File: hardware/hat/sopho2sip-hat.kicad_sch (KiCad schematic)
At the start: 52 parts, among them J1 Raspberry Pi GPIO, J2 D340 Audio, J3 D340 PC-Schnittstelle, SW1 Taste, T1 600:600, T2 600:600, U1 24LC32, U2 WM8731SEDS, U3 ADuM5211, U4 AP2112K-3.3, U5 MAX3232E, Y1 12.288MHz

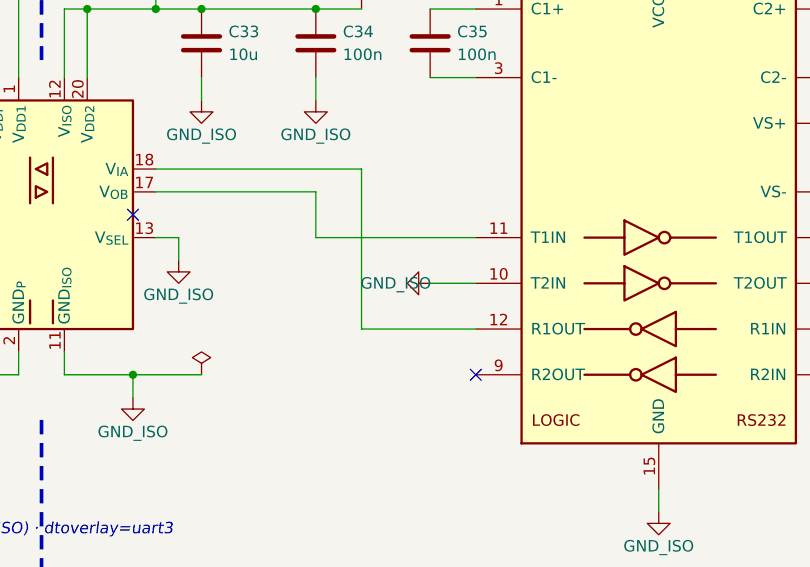
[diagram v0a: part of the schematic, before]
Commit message: CM4-Träger: hierarchischer KiCad-Schaltplan; gemeinsamer Generator kicadgen
- hardware/kicadgen.py: Symbole, Leitungen, hierarchische Blätter mit Blattpins,
  Projektbibliothek für eigene Symbole, Prüfung (ERC + Pin-Gruppen gegen SOLL)
- HAT in Blockfunktionen zerlegt (pi_leiste, hat_eeprom, codec, sprechweg, rs232,
  bedienung); Netzliste unverändert, Masse-Symbol an T2IN ohne Textüberdeckung
- hardware/cm4: Wurzelblatt mit 8 Funktionsblöcken; CM4 (DF40, GPIO_VREF, nRPIBOOT,
  Status-LEDs), USB-C-Versorgung mit rpiboot, µSD für CM4 Lite, Ethernet 10/100
  (MagJack, ESD), D340-Blöcke aus dem HAT; ERC 0/0, Netzliste 70/70
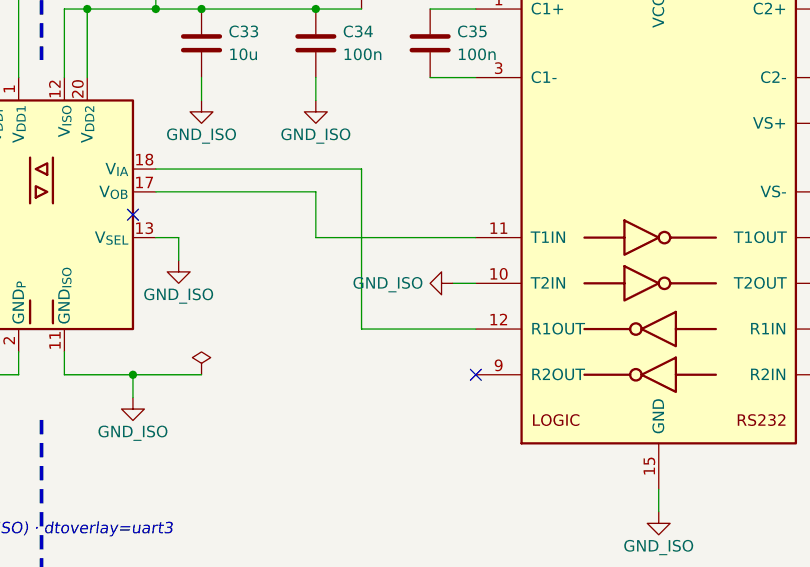
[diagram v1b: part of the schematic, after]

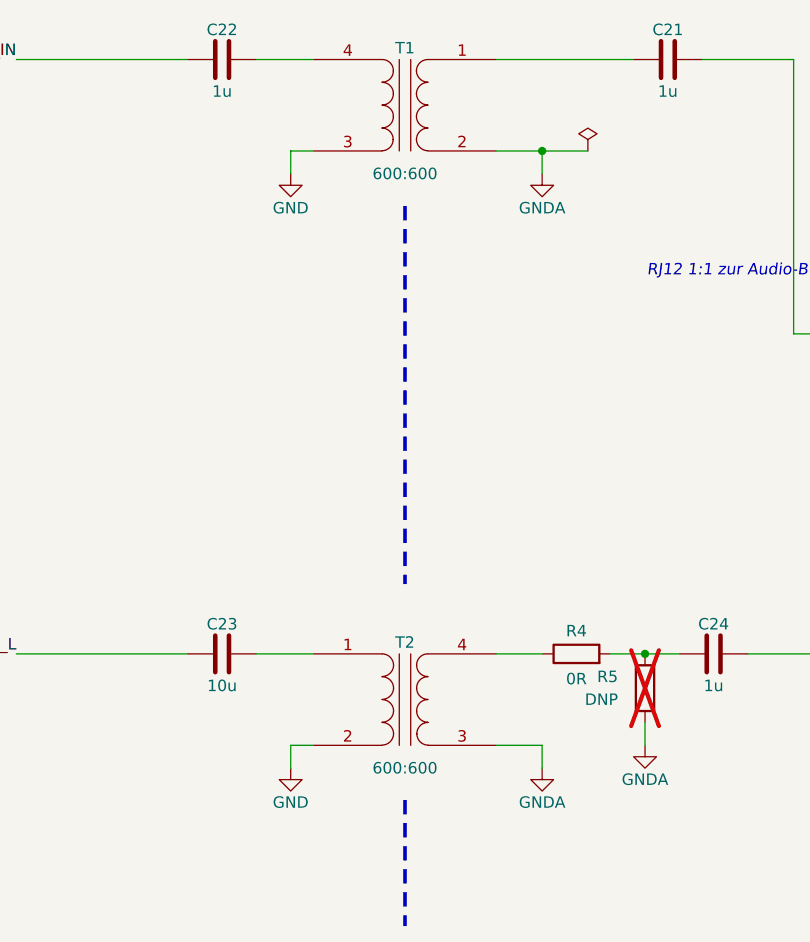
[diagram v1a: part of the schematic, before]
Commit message: CM4-Träger 0.3: Leiterplatte (4 Lagen, JLCPCB), Ein/Aus-Taster, Lüfter, lieferbare Teile
Schaltplan
- Codec TI TLV320AIC3204 statt WM8731 (abgekündigt); MCLK 12 MHz, Reset GPIO26, I²C an GPIO0/1
- Ein/Aus-Taster an GPIO3 (gpio-shutdown im Betrieb, Bootloader-Wecken im Halt)
- Lüfterblatt: AO3400A an GPIO12, Freilaufdiode, JST-PH-Anschluss; gpio-fan über SoC-Temperatur
- Konfig-Taster SW2 und Status-LED D3; Würth RJ45/RJ12, Bourns SM-LP-5001, TPD4E05U06
- reproduzierbare UUIDs (Schaltplan ↔ Platine bleiben verknüpft), eigene Footprints in hardware/bibliothek

Leiterplatte (erzeuge_layout.py)
- 110 × 85 mm, F.Cu / In1 GND / In2 +3V3 / B.Cu, JLC04161H-7628, JLCPCB-Regeln (.kicad_dru)
- CM4-Lage nach CM4IO-Referenz, Antennen-Sperrzone, isolierte Bereiche GND_ISO/GNDA mit Trennstreifen
- eigenes Fanout zu den Ebenen, Routing mit FreeRouting 1.9.0 über xvfb (2.x: Telemetrie an)
- DRC ohne Verstöße, 0 offene Verbindungen, Schaltplan ↔ Platine identisch
- Bestellliste für Digikey mit geprüftem Lagerbestand
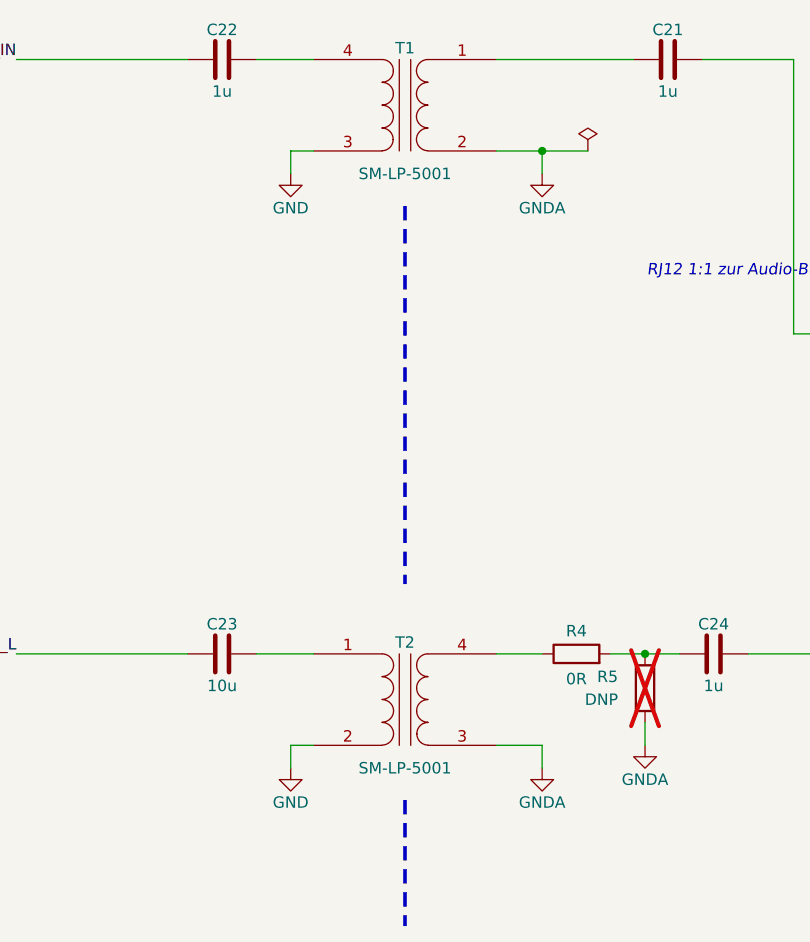
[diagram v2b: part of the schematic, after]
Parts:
- H1, H2, H3, H4: now left out of the parts list
- J2: footprint Connector_RJ:RJ12_Amphenol_54601-x06_Horizontal -> Sopho2SIP:RJ12_Wuerth_615006138421_Horizontal
- T1, T2: value 600:600 -> SM-LP-5001; footprint (none) -> Sopho2SIP:Bourns_SM-LP-5001

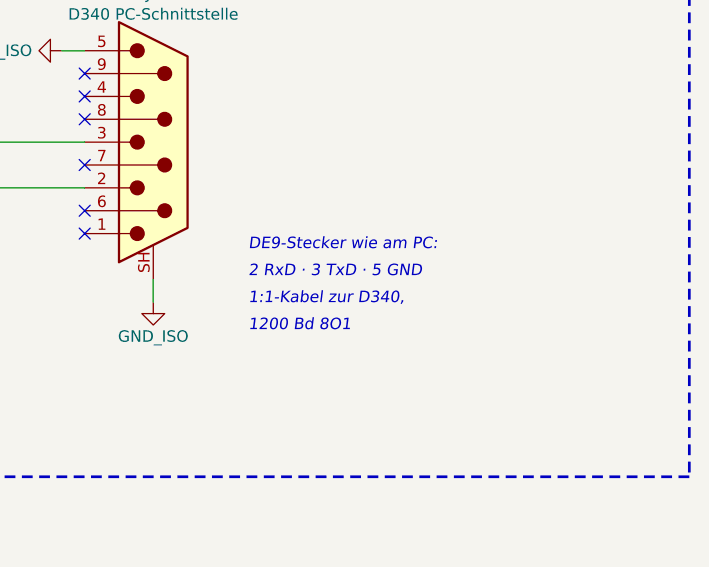
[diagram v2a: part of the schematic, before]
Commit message: Schaltplan: Hinweise als Textkästen (KiCad bricht um); Texte werden in den Generator zurückgeführt
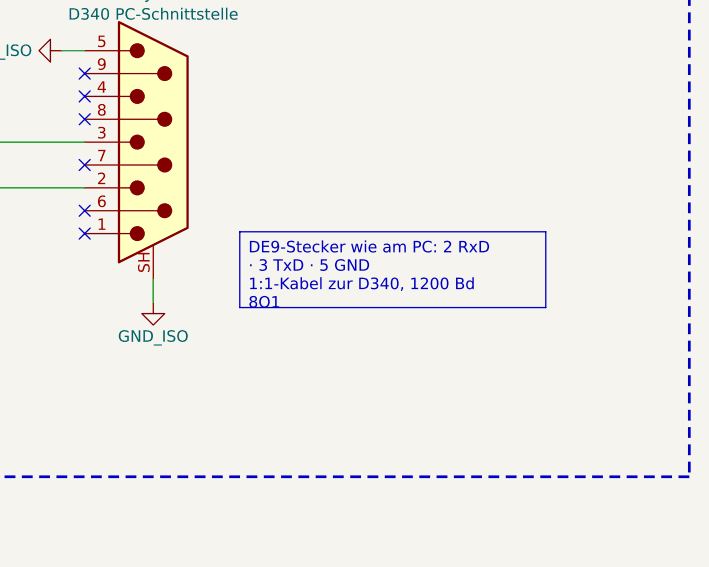
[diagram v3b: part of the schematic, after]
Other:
- note removed: "1200 Bd 8O1"
- note removed: "1:1-Kabel zur D340,"
- note removed: "2 RxD · 3 TxD · 5 GND"
- note removed: "DE9-Stecker wie am PC:"
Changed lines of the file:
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@@
 	(text "isolierte Seite (GND_ISO)" (exclude_from_sim no) (at 208 246 0) (effects (font (size 1.27 1.27) italic) (justify left bottom)))
 	(text "ADuM5211: Trenner mit isolierter 3,3-V-Versorgung (VSEL = GND_ISO) · dtoverlay=uart3" (exclude_from_sim no) (at 140 239 0) (effects (font (size 1.27 1.27) italic) (justify left bottom)))
-	(text "DE9-Stecker wie am PC:" (exclude_from_sim no) (at 356 223 0) (effects (font (size 1.27 1.27) italic) (justify left bottom)))
-	(text "2 RxD · 3 TxD · 5 GND" (exclude_from_sim no) (at 356 226 0) (effects (font (size 1.27 1.27) italic) (justify left bottom)))
-	(text "1:1-Kabel zur D340," (exclude_from_sim no) (at 356 229 0) (effects (font (size 1.27 1.27) italic) (justify left bottom)))
-	(text "1200 Bd 8O1" (exclude_from_sim no) (at 356 232 0) (effects (font (size 1.27 1.27) italic) (justify left bottom)))
+	(text_box "DE9-Stecker wie am PC: 2 RxD · 3 TxD · 5 GND\n1:1-Kabel zur D340, 1200 Bd 8O1" (exclude_from_sim no) (at 355.05 220.78 0) (size 34 8.42) (margins 0.9525 0.9525 0.9525 0.9525) (stroke (width 0.1) (type solid) (color 132 132 132 1)) (fill (type color) (color 255 255 230 1)) (effects (font (size 1.27 1.27)) (justify left top)))
 	(polyline (pts (xy 325.12 32) (xy 325.12 39)) (stroke (width 0.4) (type dash_dot) (color 194 0 0 1)))
 	(polyline (pts (xy 325.12 62) (xy 325.12 104)) (stroke (width 0.4) (type dash_dot) (color 194 0 0 1)))

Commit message: CM4-Schaltplan: Handänderungen übernommen (Handlage für 8 Blätter, 2 Texte zurückgeführt); Kastenhöhen aus gemessenen Zeichenbreiten
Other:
- note added: "ADuM5211: Trenner mit isolierter 3,3-V-Versorgung (VSEL = GND_ISO) dtoverlay=uart3"
- note removed: "ADuM5211: Trenner mit isolierter 3,3-V-Versorgung (VSEL = GND_ISO) · dtoverlay=uart3"
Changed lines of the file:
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@@
 	(text "Pi-Seite (GND)" (exclude_from_sim no) (at 150 246 0) (effects (font (size 1.27 1.27) italic) (justify left bottom)))
 	(text "isolierte Seite (GND_ISO)" (exclude_from_sim no) (at 208 246 0) (effects (font (size 1.27 1.27) italic) (justify left bottom)))
-	(text "ADuM5211: Trenner mit isolierter 3,3-V-Versorgung (VSEL = GND_ISO) · dtoverlay=uart3" (exclude_from_sim no) (at 140 239 0) (effects (font (size 1.27 1.27) italic) (justify left bottom)))
-	(text_box "DE9-Stecker wie am PC: 2 RxD · 3 TxD · 5 GND\n1:1-Kabel zur D340, 1200 Bd 8O1" (exclude_from_sim no) (at 355.05 220.78 0) (size 34 8.42) (margins 0.9525 0.9525 0.9525 0.9525) (stroke (width 0.1) (type solid) (color 132 132 132 1)) (fill (type color) (color 255 255 230 1)) (effects (font (size 1.27 1.27)) (justify left top)))
+	(text "ADuM5211:\nTrenner mit isolierter 3,3-V-Versorgung\n(VSEL = GND_ISO)\ndtoverlay=uart3" (exclude_from_sim no) (at 140 239 0) (effects (font (size 1.27 1.27) italic) (justify left bottom)))
+	(text_box "DE9-Stecker wie am PC: 2 RxD · 3 TxD · 5 GND\n1:1-Kabel zur D340, 1200 Bd 8O1" (exclude_from_sim no) (at 355.05 220.78 0) (size 34 10.46) (margins 0.9525 0.9525 0.9525 0.9525) (stroke (width 0.1) (type solid) (color 132 132 132 1)) (fill (type color) (color 255 255 230 1)) (effects (font (size 1.27 1.27)) (justify left top)))
 	(polyline (pts (xy 325.12 32) (xy 325.12 39)) (stroke (width 0.4) (type dash_dot) (color 194 0 0 1)))
 	(polyline (pts (xy 325.12 62) (xy 325.12 104)) (stroke (width 0.4) (type dash_dot) (color 194 0 0 1)))
